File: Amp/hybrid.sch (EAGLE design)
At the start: 135 parts, among them IC1 TL071P, IC2 TL071P, IC3 LM317MABT, IC4 LM317MABT, J1 NRJ3HF-1, K1 UA2-12NJ, Q1 KSP06KINKED, Q10 BD139, Q11 KSP06KINKED, Q12 BC560KINKED, Q13 BC560KINKED, Q14 BC560KINKED, Q15 BC556KINKED, Q16 BC550KINKED, Q17 BC550KINKED, Q18 BC560KINKED, Q19 BD140, Q2 BC560KINKED, Q20 BD139, Q21 KSP43, Q22 KSP43, Q23 BC546KINKED, Q3 BC560KINKED, Q4 BC560KINKED, Q5 BC556KINKED, Q6 BC550KINKED, Q7 BC550KINKED, Q8 BC560KINKED, Q9 BD140, U1 TL7700DIP-8

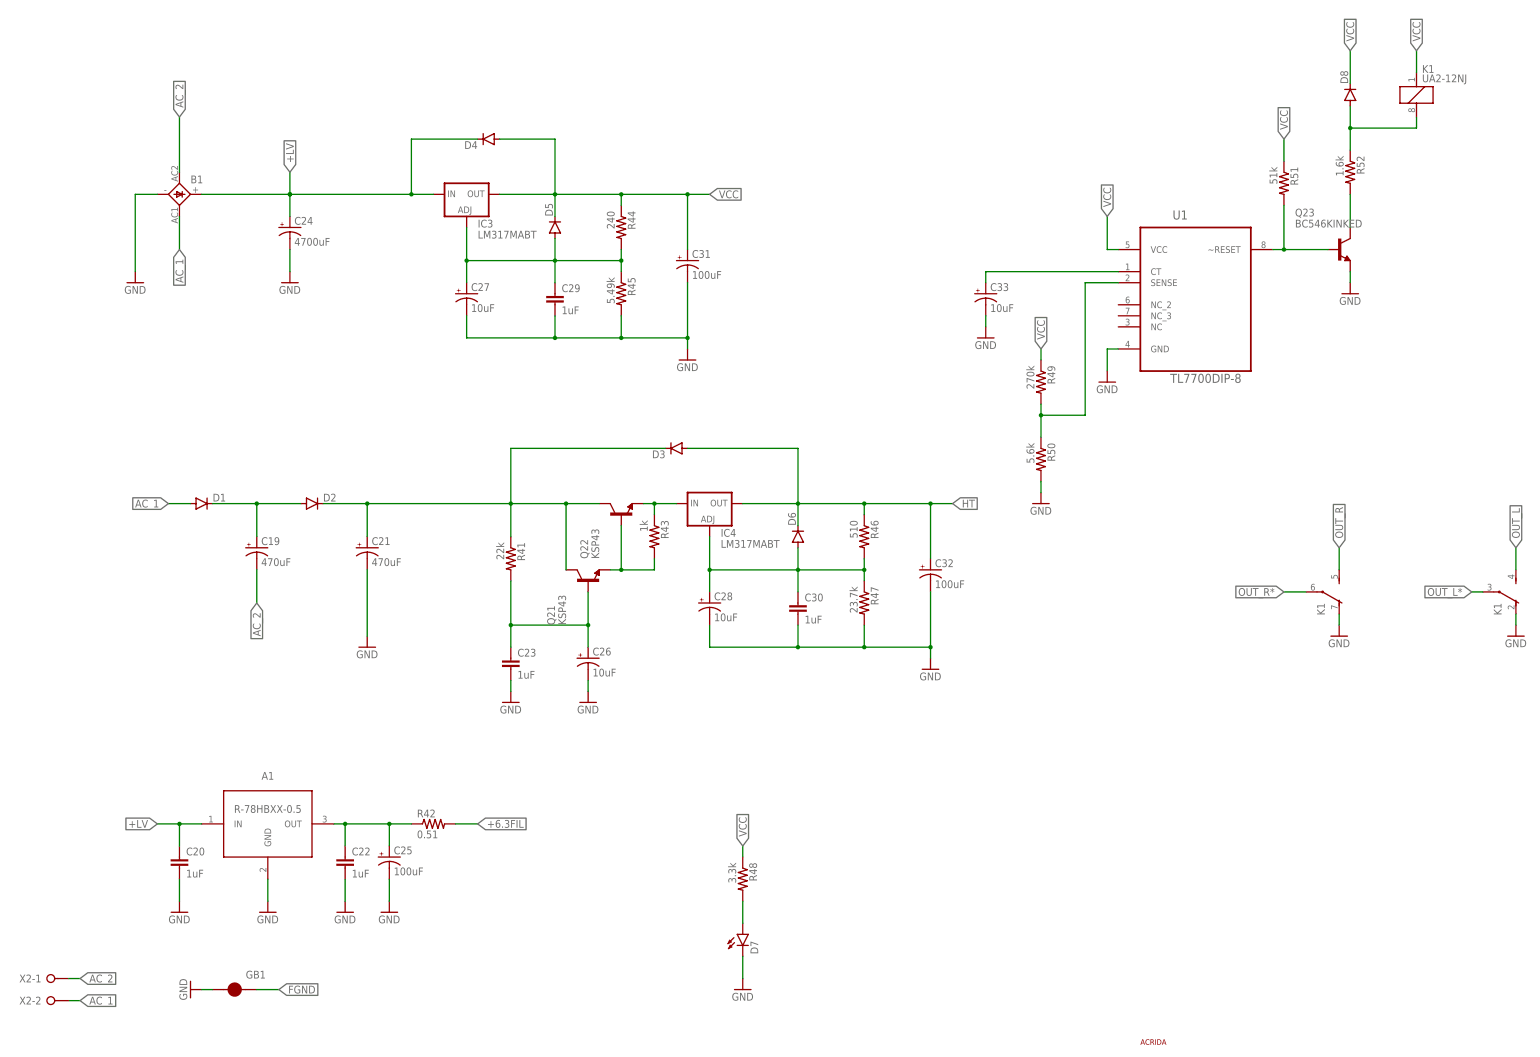
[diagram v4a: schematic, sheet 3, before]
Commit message: Capacitors polarity was reversed
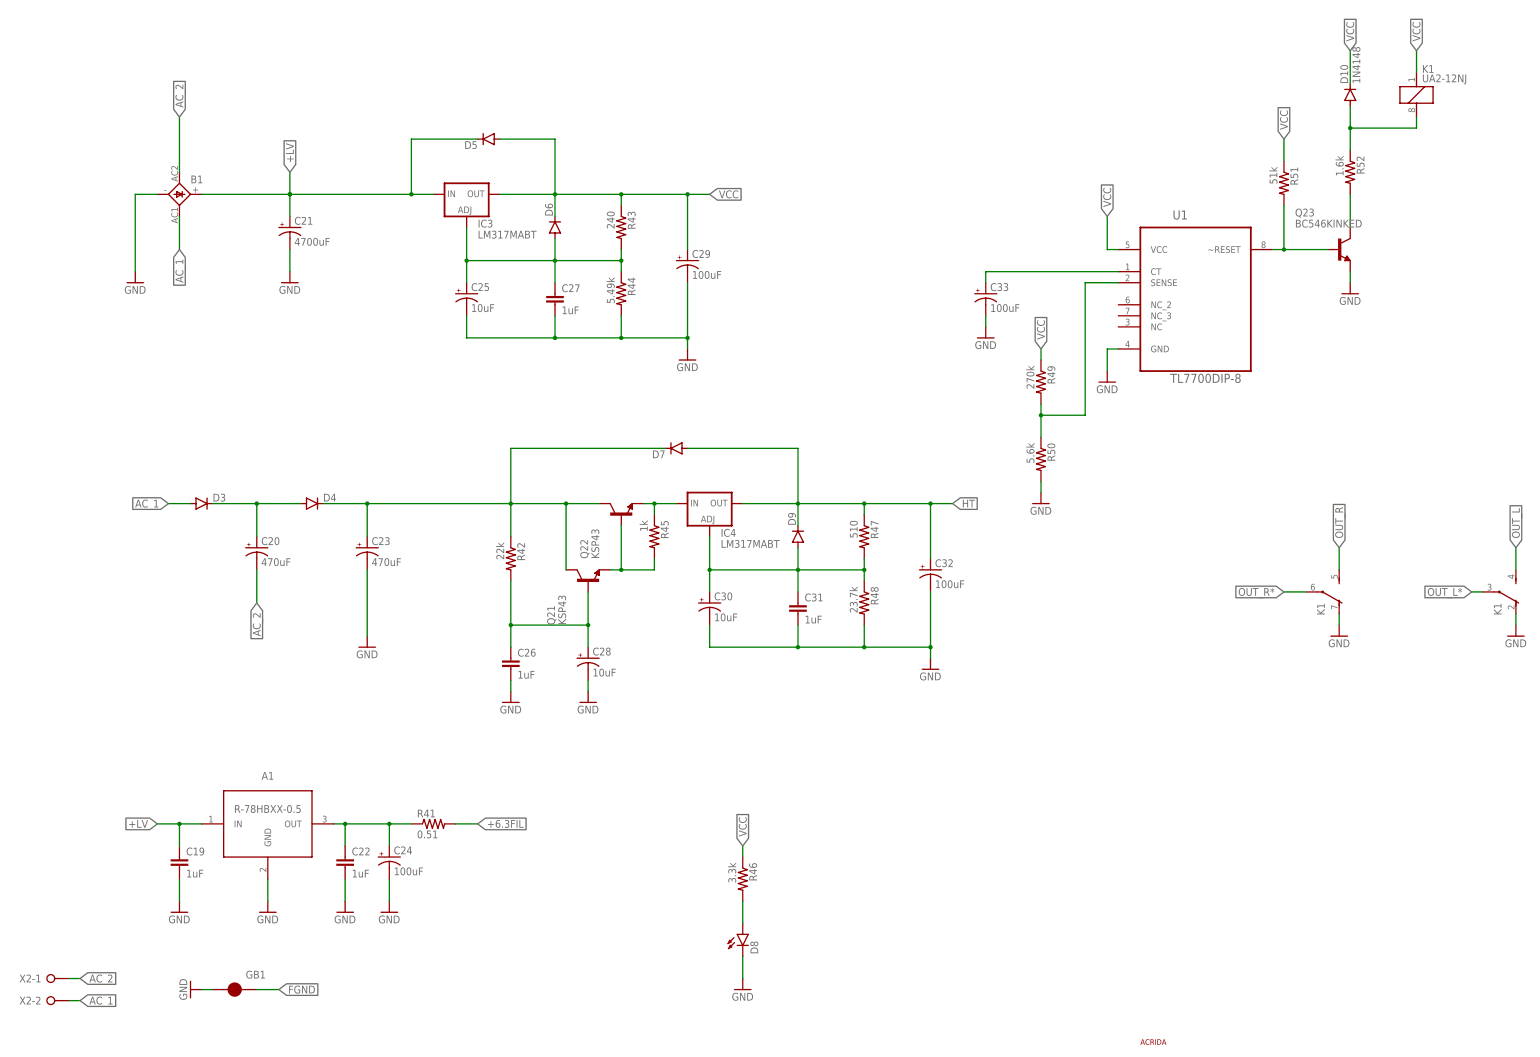
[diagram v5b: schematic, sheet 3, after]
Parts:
- added D10: 1N4148, my:DIODE1N4148
- added D9: (no value), SparkFun-DiscreteSemi:DIODEPTH
- C19: value 470uF -> 1uF; device my-cap:CAP_POLPTH-18/7.5 -> SparkFun-Capacitors:CAPPTH1
- C20, C23: value 1uF -> 470uF; device SparkFun-Capacitors:CAPPTH1 -> my-cap:CAP_POLPTH-18/7.5
- C21: value 470uF -> 4700uF; device my-cap:CAP_POLPTH-18/7.5 -> my-cap:CAP_POLSNAPIN-30/10
- C24: value 4700uF -> 100uF; device my-cap:CAP_POLSNAPIN-30/10 -> my-cap:CAP_POLPTH-6.5/2.5
- C25: value 100uF -> 10uF
- C26: value 10uF -> 1uF; device my-cap:CAP_POLPTH-12/5 -> SparkFun-Capacitors:CAPPTH1
- C27: value 10uF -> 1uF; device my-cap:CAP_POLPTH-6.5/2.5 -> SparkFun-Capacitors:CAPPTH
- C28: device my-cap:CAP_POLPTH-6.5/2.5 -> my-cap:CAP_POLPTH-12/5
- C29: value 1uF -> 100uF; device SparkFun-Capacitors:CAPPTH -> my-cap:CAP_POLPTH-12.5/5
- C30: value 1uF -> 10uF; device SparkFun-Capacitors:CAPPTH -> my-cap:CAP_POLPTH-6.5/2.5
- C31: value 100uF -> 1uF; device my-cap:CAP_POLPTH-12.5/5 -> SparkFun-Capacitors:CAPPTH
- C33: value 10uF -> 100uF
- D1, D2: value (none) -> 1N4148; device SparkFun-DiscreteSemi:DIODEPTH -> my:DIODE1N4148
- D7: device SparkFun-LED:LED3MM -> SparkFun-DiscreteSemi:DIODEPTH
- D8: device SparkFun-DiscreteSemi:DIODEKIT -> SparkFun-LED:LED3MM
- R41: value 22k -> 0.51; device SparkFun-Resistors:RESISTORPTH-1/4W -> my-res:RESISTORPTH-1/2W
- R42: value 0.51 -> 22k; device my-res:RESISTORPTH-1/2W -> SparkFun-Resistors:RESISTORPTH-1/4W
- R43: value 1k -> 240
- R44: value 240 -> 5.49k
- R45: value 5.49k -> 1k
- R46: value 510 -> 3.3k
- R47: value 23.7k -> 510
- R48: value 3.3k -> 23.7k
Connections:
- net +6.3FIL: now also R41.2; no longer R42.2
- net +LV: now also C19.1, C21.+, D5.C; no longer C20.1, C24.+, D4.C
- net AC_1: now also D3.A; no longer D1.A
- net AC_2: now also C20.-; no longer C19.-
- net FB_L: now also C5.+, D1.C; no longer C5.-
- net FB_R: now also C14.+, D2.C; no longer C14.-
- net GND: now also C19.2, C23.-, C26.2, C27.2, C29.-, C30.-, C31.2, D8.C, R44.2, R48.2; no longer C20.2, C23.2, C26.-, C27.-, C29.2, C30.2, C31.-, D7.C, R45.2, R47.2
- net HT: now also D7.A, D9.C, R47.1; no longer D3.A, D6.C, R46.1
- net N$18: now also R45.2; no longer R43.2
- net N$19: now also C14.-, D2.A; no longer C14.+
- net N$30: now also C25.+, C27.1, D6.A, R43.2, R44.1; no longer C27.+, C29.1, D5.A, R44.2, R45.1
- net N$31: now also C20.+, D3.C, D4.A; no longer C19.+, D1.C, D2.A
- net N$32: now also C24.+, R41.1; no longer C25.+, R42.1
- net N$33: now also C23.+, D4.C, D7.C, R42.1; no longer C21.+, D2.C, D3.C, R41.1
- net N$34: now also C26.1, C28.+, R42.2; no longer C23.1, C26.+, R41.2
- net N$36: now also C30.+, C31.1, D9.A, R47.2, R48.1; no longer C28.+, C30.1, D6.A, R46.2, R47.1
- net N$37: now also R45.1; no longer R43.1
- net N$4: now also C5.-, D1.A; no longer C5.+
- net N$46: now also D8.A, R46.2; no longer D7.A, R48.2
- net N$49: now also D10.A; no longer D8.A
- net VCC: now also C29.+, D10.C, D5.A, D6.C, R43.1, R46.1; no longer C31.+, D4.A, D5.C, D8.C, R44.1, R48.1
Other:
- moved on the sheet: C14, C21, C24, C25, C28, C5, D3, D4, D5, D6, R41, R42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

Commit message: Use snap in caps
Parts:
- C20, C23: device my-cap:CAP_POLPTH-18/7.5 -> my-cap:CAP_POLSNAPIN-22/10
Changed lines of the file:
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@@
 <part name="D5" library="SparkFun-DiscreteSemi" deviceset="DIODE" device="PTH"/>
 <part name="C29" library="my-cap" deviceset="CAP_POL" device="PTH-12.5/5" value="100uF"/>
-<part name="C20" library="my-cap" deviceset="CAP_POL" device="PTH-18/7.5" value="470uF"/>
-<part name="C23" library="my-cap" deviceset="CAP_POL" device="PTH-18/7.5" value="470uF"/>
+<part name="C20" library="my-cap" deviceset="CAP_POL" device="SNAPIN-22/10" value="470uF"/>
+<part name="C23" library="my-cap" deviceset="CAP_POL" device="SNAPIN-22/10" value="470uF"/>
 <part name="D4" library="SparkFun-DiscreteSemi" deviceset="DIODE" device="PTH"/>
 <part name="D3" library="SparkFun-DiscreteSemi" deviceset="DIODE" device="PTH"/>

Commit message: Small adjustments
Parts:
- IC1, IC2: device linear:TL071P -> my-ic:TL071P
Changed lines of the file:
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@@
 <part name="R6" library="SparkFun-Resistors" deviceset="RESISTOR" device="PTH-1/4W" value="330"/>
 <part name="C3" library="capacitor-wima" deviceset="C" device="5/5" value="1uF"/>
-<part name="IC1" library="linear" deviceset="TL071" device="P"/>
+<part name="IC1" library="my-ic" deviceset="TL071" device="P"/>
 <part name="GND6" library="SparkFun-Aesthetics" deviceset="GND" device=""/>
 <part name="R2" library="SparkFun-Resistors" deviceset="RESISTOR" device="PTH-1/4W" value="2Meg"/>
@@
 <part name="GND9" library="SparkFun-Aesthetics" deviceset="GND" device=""/>
 <part name="C11" library="capacitor-wima" deviceset="C" device="5/5" value="1uF"/>
-<part name="IC2" library="linear" deviceset="TL071" device="P"/>
+<part name="IC2" library="my-ic" deviceset="TL071" device="P"/>
 <part name="GND20" library="SparkFun-Aesthetics" deviceset="GND" device=""/>
 <part name="R22" library="SparkFun-Resistors" deviceset="RESISTOR" device="PTH-1/4W" value="2Meg"/>
